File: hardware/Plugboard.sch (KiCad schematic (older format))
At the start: 1 part

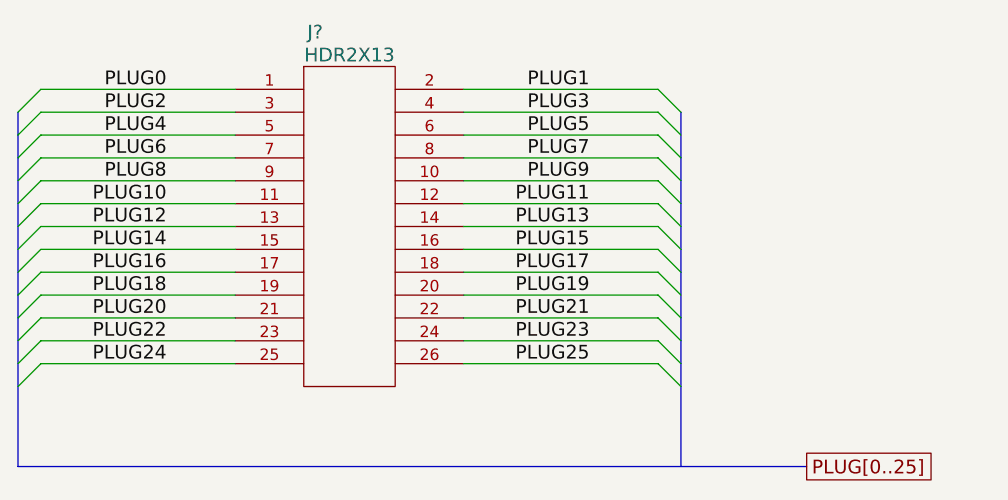
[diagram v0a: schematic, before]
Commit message: 
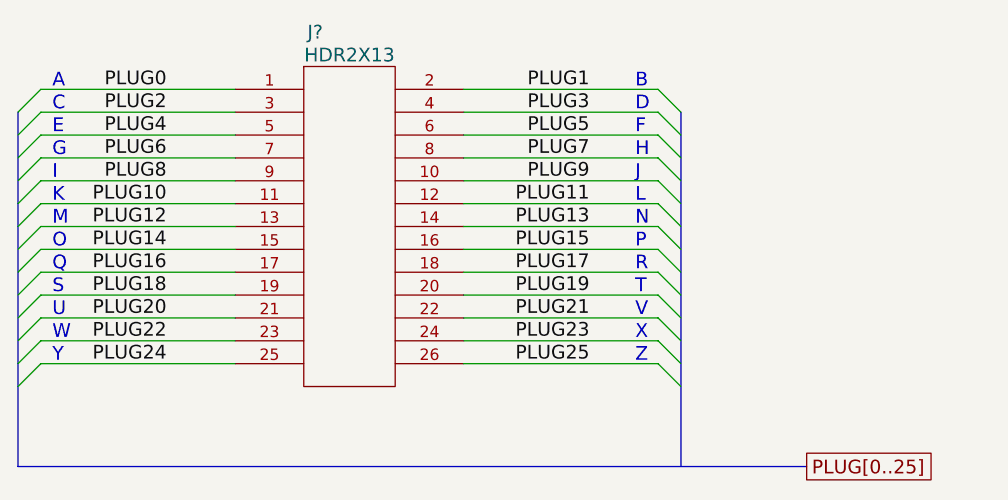
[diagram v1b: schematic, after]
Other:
- note added: "A"
- note added: "B"
- note added: "C"
- note added: "D"
- note added: "E"
- note added: "F"
- note added: "G"
- note added: "H"
- note added: "I"
- note added: "J"
- note added: "K"
- note added: "L"
- note added: "M"
- note added: "N"
- note added: "O"
- note added: "P"
- note added: "Q"
- note added: "R"
- note added: "S"
- note added: "T"
- note added: "U"
- note added: "V"
- note added: "W"
- note added: "X"
- note added: "Y"
- note added: "Z"
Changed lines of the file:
@@
-EESchema Schematic File Version 2  date Mon 24 Mar 2014 21:55:02 GMT
+EESchema Schematic File Version 2  date Tue 25 Mar 2014 19:29:54 GMT
 LIBS:power
 LIBS:device
@@
 LIBS:valves
 LIBS:enigma_board
+LIBS:topsheet-cache
 EELAYER 25  0
 EELAYER END
@@
 Sheet 3 7
 Title ""
-Date "24 mar 2014"
+Date "25 mar 2014"
 Rev ""
 Comp ""
@@
 Comment4 ""
 $EndDescr
+Text Notes 7000 4450 0    60   ~ 0
+Z
+Text Notes 4450 4450 0    60   ~ 0
+Y
+Text Notes 7000 4350 0    60   ~ 0
+X
+Text Notes 4450 4350 0    60   ~ 0
+W
+Text Notes 7000 4250 0    60   ~ 0
+V
+Text Notes 4450 4250 0    60   ~ 0
+U
+Text Notes 7000 4150 0    60   ~ 0
+T
+Text Notes 4450 4150 0    60   ~ 0
+S
+Text Notes 7000 4050 0    60   ~ 0
+R
+Text Notes 4450 4050 0    60   ~ 0
+Q
+Text Notes 7000 3950 0    60   ~ 0
+P
+Text Notes 4450 3950 0    60   ~ 0
+O
+Text Notes 7000 3850 0    60   ~ 0
+N
+Text Notes 4450 3850 0    60   ~ 0
+M
+Text Notes 7000 3750 0    60   ~ 0
+L
+Text Notes 4450 3750 0    60   ~ 0
+K
+Text Notes 7000 3650 0    60   ~ 0
+J
+Text Notes 4450 3650 0    60   ~ 0
+I
+Text Notes 7000 3550 0    60   ~ 0
+H
+Text Notes 4450 3550 0    60   ~ 0
+G
+Text Notes 7000 3450 0    60   ~ 0
+F
+Text Notes 4450 3450 0    60   ~ 0
+E
+Text Notes 7000 3350 0    60   ~ 0
+D
+Text Notes 4450 3350 0    60   ~ 0
+C
+Text Notes 7000 3250 0    60   ~ 0
+B
+Text Notes 4450 3250 0    60   ~ 0
+A
 Text GLabel 7750 4900 2    60   UnSpc ~ 0
 PLUG[0..25]
